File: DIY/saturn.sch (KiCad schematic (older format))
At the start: 7 parts, among them J1 Conn_01x09, J2 Conn_01x09, J3 DB25_Male, U1 74AHCT125N, U2 74AHCT125N, U3 74AHCT125N, U4 74AHCT125N

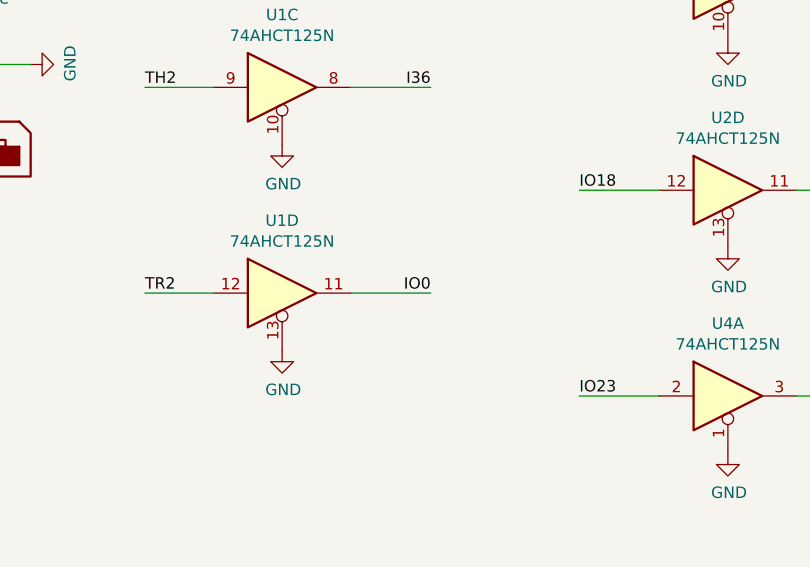
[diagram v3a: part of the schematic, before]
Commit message: Update adapter cable schematics
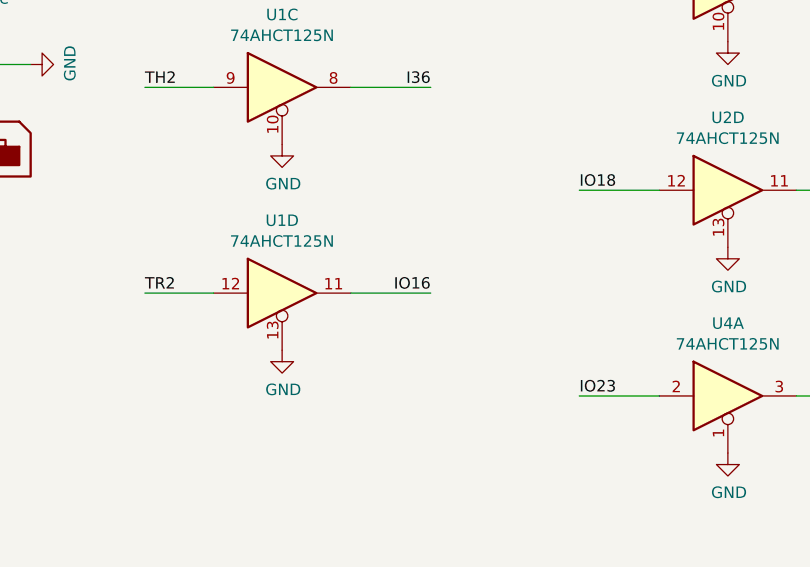
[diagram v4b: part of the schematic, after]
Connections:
- net IO0 is gone; now on net IO16: U1.11
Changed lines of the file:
@@
 $Descr USLetter 11000 8500
 encoding utf-8
-Sheet 2 7
+Sheet 2 10
 Title "BlueRetro - Saturn adapter cable"
-Date "2020-10-02"
-Rev "v1.2"
+Date "2020-11-01"
+Rev "v1.2.1"
 Comp "©2020 Jacques Gagnon, licensed under CC-BY-4.0"
 Comment1 ""
@@
 	9050 2300 9350 2300
 $Comp
-L power:+5V #PWR?
+L power:+5V #PWR042
 U 1 1 5F1A0B4B
 P 9250 1600
-F 0 "#PWR?" H 9250 1450 50  0001 C CNN
+F 0 "#PWR042" H 9250 1450 50  0001 C CNN
 F 1 "+5V" H 9265 1773 50  0000 C CNN
 F 2 "" H 9250 1600 50  0001 C CNN
@@
 $EndComp
 $Comp
-L power:GND #PWR?
+L power:GND #PWR040
 U 1 1 5F1A1AF6
 P 9150 4200
-F 0 "#PWR?" H 9150 3950 50  0001 C CNN
+F 0 "#PWR040" H 9150 3950 50  0001 C CNN
 F 1 "GND" H 9155 4027 50  0000 C CNN
 F 2 "" H 9150 4200 50  0001 C CNN
@@
 	9250 2900 9350 2900
 $Comp
-L power:+3.3V #PWR?
+L power:+3.3V #PWR039
 U 1 1 5F1B1DC0
 P 8950 2650
-F 0 "#PWR?" H 8950 2500 50  0001 C CNN
+F 0 "#PWR039" H 8950 2500 50  0001 C CNN
 F 1 "+3.3V" H 8965 2823 50  0000 C CNN
 F 2 "" H 8950 2650 50  0001 C CNN
@@
 $EndComp
 $Comp
-L power:GND #PWR?
+L power:GND #PWR030
 U 1 1 5F1BE190
 P 5000 4300
-F 0 "#PWR?" H 5000 4050 50  0001 C CNN
+F 0 "#PWR030" H 5000 4050 50  0001 C CNN
 F 1 "GND" H 5005 4127 50  0000 C CNN
 F 2 "" H 5000 4300 50  0001 C CNN
@@
 $EndComp
 $Comp
-L power:GND #PWR?
+L power:GND #PWR029
 U 1 1 5F1BE7CF
 P 5000 3400
-F 0 "#PWR?" H 5000 3150 50  0001 C CNN
+F 0 "#PWR029" H 5000 3150 50  0001 C CNN
 F 1 "GND" H 5005 3227 50  0000 C CNN
 F 2 "" H 5000 3400 50  0001 C CNN
@@
 $EndComp
 $Comp
-L power:GND #PWR?
+L power:GND #PWR027
 U 1 1 5F1BEBDB
 P 5000 1600
-F 0 "#PWR?" H 5000 1350 50  0001 C CNN
+F 0 "#PWR027" H 5000 1350 50  0001 C CNN
 F 1 "GND" H 5005 1427 50  0000 C CNN
 F 2 "" H 5000 1600 50  0001 C CNN
@@
 $EndComp
 $Comp
-L power:GND #PWR?
+L power:GND #PWR028
 U 1 1 5F1BEFCD
 P 5000 2500
-F 0 "#PWR?" H 5000 2250 50  0001 C CNN
+F 0 "#PWR028" H 5000 2250 50  0001 C CNN
 F 1 "GND" H 5005 2327 50  0000 C CNN
 F 2 "" H 5000 2500 50  0001 C CNN
@@
 $EndComp
 $Comp
-L power:GND #PWR?
+L power:GND #PWR020
 U 1 1 5F1C0216
 P 3050 2950
-F 0 "#PWR?" H 3050 2700 50  0001 C CNN
+F 0 "#PWR020" H 3050 2700 50  0001 C CNN
 F 1 "GND" H 3055 2777 50  0000 C CNN
 F 2 "" H 3050 2950 50  0001 C CNN
@@
 $EndComp
 $Comp
-L power:GND #PWR?
+L power:GND #PWR022
 U 1 1 5F1C070C
 P 3050 4750
-F 0 "#PWR?" H 3050 4500 50  0001 C CNN
+F 0 "#PWR022" H 3050 4500 50  0001 C CNN
 F 1 "GND" H 3055 4577 50  0000 C CNN
 F 2 "" H 3050 4750 50  0001 C CNN
@@
 $EndComp
 $Comp
-L power:GND #PWR?
+L power:GND #PWR019
 U 1 1 5F1C2C4C
 P 3050 2050
-F 0 "#PWR?" H 3050 1800 50  0001 C CNN
+F 0 "#PWR019" H 3050 1800 50  0001 C CNN
 F 1 "GND" H 3055 1877 50  0000 C CNN
 F 2 "" H 3050 2050 50  0001 C CNN
@@
 $EndComp
 $Comp
-L power:GND #PWR?
+L power:GND #PWR021
 U 1 1 5F1C2FA8
 P 3050 3850
-F 0 "#PWR?" H 3050 3600 50  0001 C CNN
+F 0 "#PWR021" H 3050 3600 50  0001 C CNN
 F 1 "GND" H 3055 3677 50  0000 C CNN
 F 2 "" H 3050 3850 50  0001 C CNN
@@
 $EndComp
 $Comp
-L power:GND #PWR?
+L power:GND #PWR032
 U 1 1 5F1C38EA
 P 7000 1600
-F 0 "#PWR?" H 7000 1350 50  0001 C CNN
+F 0 "#PWR032" H 7000 1350 50  0001 C CNN
 F 1 "GND" H 7005 1427 50  0000 C CNN
 F 2 "" H 7000 1600 50  0001 C CNN
@@
 $EndComp
 $Comp
-L power:GND #PWR?
+L power:GND #PWR034
 U 1 1 5F1C472F
 P 7000 3400
-F 0 "#PWR?" H 7000 3150 50  0001 C CNN
+F 0 "#PWR034" H 7000 3150 50  0001 C CNN
 F 1 "GND" H 7005 3227 50  0000 C CNN
 F 2 "" H 7000 3400 50  0001 C CNN
@@
 $EndComp
 $Comp
-L power:GND #PWR?
+L power:GND #PWR033
 U 1 1 5F1C4BA8
 P 7000 2500
-F 0 "#PWR?" H 7000 2250 50  0001 C CNN
+F 0 "#PWR033" H 7000 2250 50  0001 C CNN
 F 1 "GND" H 7005 2327 50  0000 C CNN
 F 2 "" H 7000 2500 50  0001 C CNN
@@
 $EndComp
 $Comp
-L power:GND #PWR?
+L power:GND #PWR035
 U 1 1 5F1C4F7E
 P 7000 4300
-F 0 "#PWR?" H 7000 4050 50  0001 C CNN
+F 0 "#PWR035" H 7000 4050 50  0001 C CNN
 F 1 "GND" H 7005 4127 50  0000 C CNN
 F 2 "" H 7000 4300 50  0001 C CNN
@@
 $EndComp
 $Comp
-L power:GND #PWR?
+L power:GND #PWR031
 U 1 1 5F1C70A0
 P 5000 5200
-F 0 "#PWR?" H 5000 4950 50  0001 C CNN
+F 0 "#PWR031" H 5000 4950 50  0001 C CNN
 F 1 "GND" H 5005 5027 50  0000 C CNN
 F 2 "" H 5000 5200 50  0001 C CNN
@@
 $EndComp
 $Comp
-L power:GND #PWR?
+L power:GND #PWR038
 U 1 1 5F1C7615
 P 8450 6100
-F 0 "#PWR?" H 8450 5850 50  0001 C CNN
+F 0 "#PWR038" H 8450 5850 50  0001 C CNN
 F 1 "GND" H 8455 5927 50  0000 C CNN
 F 2 "" H 8450 6100 50  0001 C CNN
@@
 $EndComp
 $Comp
-L power:GND #PWR?
+L power:GND #PWR043
 U 1 1 5F1C7B22
 P 9500 6100
-F 0 "#PWR?" H 9500 5850 50  0001 C CNN
+F 0 "#PWR043" H 9500 5850 50  0001 C CNN
 F 1 "GND" H 9505 5927 50  0000 C CNN
 F 2 "" H 9500 6100 50  0001 C CNN
@@
 $EndComp
 $Comp
-L power:GND #PWR?
+L power:GND #PWR036
 U 1 1 5F1C815E
 P 7000 5200
-F 0 "#PWR?" H 7000 4950 50  0001 C CNN
+F 0 "#PWR036" H 7000 4950 50  0001 C CNN
 F 1 "GND" H 7005 5027 50  0000 C CNN
 F 2 "" H 7000 5200 50  0001 C CNN
@@
 $EndComp
 $Comp
-L power:GND #PWR?
+L power:GND #PWR014
 U 1 1 5F1CC3E3
 P 1500 7100
-F 0 "#PWR?" H 1500 6850 50  0001 C CNN
+F 0 "#PWR014" H 1500 6850 50  0001 C CNN
 F 1 "GND" H 1505 6927 50  0000 C CNN
 F 2 "" H 1500 7100 50  0001 C CNN
@@
 $EndComp
 $Comp
-L power:GND #PWR?
+L power:GND #PWR026
 U 1 1 5F1CCBB0
 P 4800 7100
-F 0 "#PWR?" H 4800 6850 50  0001 C CNN
+F 0 "#PWR026" H 4800 6850 50  0001 C CNN
 F 1 "GND" H 4805 6927 50  0000 C CNN
 F 2 "" H 4800 7100 50  0001 C CNN
@@
 $EndComp
 $Comp
-L power:GND #PWR?
+L power:GND #PWR024
 U 1 1 5F1CEDC5
 P 3850 7100
-F 0 "#PWR?" H 3850 6850 50  0001 C CNN
+F 0 "#PWR024" H 3850 6850 50  0001 C CNN
 F 1 "GND" H 3855 6927 50  0000 C CNN
 F 2 "" H 3850 7100 50  0001 C CNN
@@
 $EndComp
 $Comp
-L power:GND #PWR?
+L power:GND #PWR018
 U 1 1 5F1CF2C2
 P 2900 7100
-F 0 "#PWR?" H 2900 6850 50  0001 C CNN
+F 0 "#PWR018" H 2900 6850 50  0001 C CNN
 F 1 "GND" H 2905 6927 50  0000 C CNN
 F 2 "" H 2900 7100 50  0001 C CNN
@@
 $EndComp
 $Comp
-L power:+3.3V #PWR?
+L power:+3.3V #PWR013
 U 1 1 5F1D27FF
 P 1500 6100
-F 0 "#PWR?" H 1500 5950 50  0001 C CNN
+F 0 "#PWR013" H 1500 5950 50  0001 C CNN
 F 1 "+3.3V" H 1515 6273 50  0000 C CNN
 F 2 "" H 1500 6100 50  0001 C CNN
@@
 $EndComp
 $Comp
-L power:+5V #PWR?
+L power:+5V #PWR023
 U 1 1 5F1D7D77
 P 3850 6100
-F 0 "#PWR?" H 3850 5950 50  0001 C CNN
+F 0 "#PWR023" H 3850 5950 50  0001 C CNN
 F 1 "+5V" H 3865 6273 50  0000 C CNN
 F 2 "" H 3850 6100 50  0001 C CNN
@@
 $EndComp
 $Comp
-L power:+5V #PWR?
+L power:+5V #PWR017
 U 1 1 5F1DBE8C
 P 2900 6100
-F 0 "#PWR?" H 2900 5950 50  0001 C CNN
+F 0 "#PWR017" H 2900 5950 50  0001 C CNN
 F 1 "+5V" H 2915 6273 50  0000 C CNN
 F 2 "" H 2900 6100 50  0001 C CNN
@@
 $EndComp
 $Comp
-L power:+5V #PWR?
+L power:+5V #PWR025
 U 1 1 5F1E0313
 P 4800 6100
-F 0 "#PWR?" H 4800 5950 50  0001 C CNN
+F 0 "#PWR025" H 4800 5950 50  0001 C CNN
 F 1 "+5V" H 4815 6273 50  0000 C CNN
 F 2 "" H 4800 6100 50  0001 C CNN
@@
 NoConn ~ 9800 5850
 $Comp
-L power:GND #PWR?
+L power:GND #PWR041
 U 1 1 5F30ECE4
 P 9200 5850
-F 0 "#PWR?" H 9200 5600 50  0001 C CNN
+F 0 "#PWR041" H 9200 5600 50  0001 C CNN
 F 1 "GND" H 9205 5677 50  0000 C CNN
 F 2 "" H 9200 5850 50  0001 C CNN
@@
 $EndComp
 $Comp
-L power:GND #PWR?
+L power:GND #PWR037
 U 1 1 5F30F0E0
 P 8150 5850
-F 0 "#PWR?" H 8150 5600 50  0001 C CNN
+F 0 "#PWR037" H 8150 5600 50  0001 C CNN
 F 1 "GND" H 8155 5677 50  0000 C CNN
 F 2 "" H 8150 5850 50  0001 C CNN
@@
 I36
 Text Label 3700 4500 2    50   ~ 0
-IO0
+IO16
 Wire Wire Line
 	4700 1350 4350 1350
@@
 $EndComp
 $Comp
-L power:GND #PWR?
+L power:GND #PWR015
 U 1 1 5F3B346E
 P 1950 2650
-F 0 "#PWR?" H 1950 2400 50  0001 C CNN
+F 0 "#PWR015" H 1950 2400 50  0001 C CNN
 F 1 "GND" H 1955 2477 50  0000 C CNN
 F 2 "" H 1950 2650 50  0001 C CNN
@@
 $EndComp
 $Comp
-L power:GND #PWR?
+L power:GND #PWR016
 U 1 1 5F3B3833
 P 1950 3500
-F 0 "#PWR?" H 1950 3250 50  0001 C CNN
+F 0 "#PWR016" H 1950 3250 50  0001 C CNN
 F 1 "GND" H 1955 3327 50  0000 C CNN
 F 2 "" H 1950 3500 50  0001 C CNN
@@
 $EndComp
 $Comp
-L power:+5V #PWR?
+L power:+5V #PWR012
 U 1 1 5F3B5AF6
 P 850 3450
-F 0 "#PWR?" H 850 3300 50  0001 C CNN
+F 0 "#PWR012" H 850 3300 50  0001 C CNN
 F 1 "+5V" H 865 3623 50  0000 C CNN
 F 2 "" H 850 3450 50  0001 C CNN
@@
 $EndComp
 $Comp
-L power:+5V #PWR?
+L power:+5V #PWR011
 U 1 1 5F3B6FDE
 P 850 2600
-F 0 "#PWR?" H 850 2450 50  0001 C CNN
+F 0 "#PWR011" H 850 2450 50  0001 C CNN
 F 1 "+5V" H 865 2773 50  0000 C CNN
 F 2 "" H 850 2600 50  0001 C CNN
